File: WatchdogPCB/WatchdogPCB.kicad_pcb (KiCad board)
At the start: 2 copper layers, 5 parts, among them J1 Conn_01x05_Socket, J2 Conn_01x05_Pin, J3 Screw_Terminal_01x03, J4 Power

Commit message: Layout mostly done
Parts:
- added D1: 5.1V, Diode_THT:D_A-405_P10.16mm_Horizontal, F.Cu at (101.6, 94.0)
- added D2: 1N5404, Diode_THT:D_DO-201AD_P15.24mm_Horizontal, F.Cu at (127.0, 38.1)
- added F1: 3A, Fuse:Fuse_Blade_ATO_directSolder, F.Cu at (103.3, 38.1)
- added H1: MountingHole, MountingHole:MountingHole_3.2mm_M3_Pad, F.Cu at (147.3, 109.2)
- added H2: MountingHole, MountingHole:MountingHole_3.2mm_M3_Pad, F.Cu at (104.1, 106.7)
- added H3: MountingHole, MountingHole:MountingHole_3.2mm_M3_Pad, F.Cu at (144.8, 38.1)
- added H4: MountingHole, MountingHole:MountingHole_3.2mm_M3_Pad, F.Cu at (91.4, 55.9)
- added J5: Thermistor 1, TerminalBlock:TerminalBlock_bornier-2_P5.08mm, F.Cu at (83.8, 99.1)
- added J6: Thermistor 2, TerminalBlock:TerminalBlock_bornier-2_P5.08mm, F.Cu at (83.8, 109.2)
- added J7: Dashboard A, Connector_JST:JST_XH_B3B-XH-A_1x03_P2.50mm_Vertical, F.Cu at (147.3, 78.7)
- added J8: Dashboard B, Connector_JST:JST_XH_B5B-XH-A_1x05_P2.50mm_Vertical, F.Cu at (147.3, 96.4)
- added JP1: 5V jumper, Connector_PinSocket_2.54mm:PinSocket_1x02_P2.54mm_Vertical, F.Cu at (137.2, 63.5)
- added JP2: 12V jumper, Connector_PinSocket_2.54mm:PinSocket_1x02_P2.54mm_Vertical, F.Cu at (132.1, 40.6)
- added R1: 4.7k, Resistor_THT:R_Axial_DIN0207_L6.3mm_D2.5mm_P7.62mm_Horizontal, F.Cu at (101.6, 48.3)
- added R10: 470, Resistor_THT:R_Axial_DIN0207_L6.3mm_D2.5mm_P7.62mm_Horizontal, F.Cu at (134.6, 99.1)
- added R11: 4.7k, Resistor_THT:R_Axial_DIN0207_L6.3mm_D2.5mm_P7.62mm_Horizontal, F.Cu at (137.2, 99.1)
- added R12: 4.7k, Resistor_THT:R_Axial_DIN0207_L6.3mm_D2.5mm_P7.62mm_Horizontal, F.Cu at (142.2, 96.5)
- added R2: 1k, Resistor_THT:R_Axial_DIN0207_L6.3mm_D2.5mm_P7.62mm_Horizontal, F.Cu at (88.9, 94.0)
- added R3: 120k, Resistor_THT:R_Axial_DIN0207_L6.3mm_D2.5mm_P7.62mm_Horizontal, F.Cu at (106.7, 48.3)
- added R4: 4.7k, Resistor_THT:R_Axial_DIN0207_L6.3mm_D2.5mm_P7.62mm_Horizontal, F.Cu at (91.4, 94.0)
- added R5: 100k, Resistor_THT:R_Axial_DIN0207_L6.3mm_D2.5mm_P7.62mm_Horizontal, F.Cu at (121.9, 88.9)
- added R6: 39k, Resistor_THT:R_Axial_DIN0207_L6.3mm_D2.5mm_P7.62mm_Horizontal, F.Cu at (119.4, 96.5)
- added R7: 1k, Resistor_THT:R_Axial_DIN0207_L6.3mm_D2.5mm_P7.62mm_Horizontal, F.Cu at (124.5, 101.6)
- added R8: 1k, Resistor_THT:R_Axial_DIN0207_L6.3mm_D2.5mm_P7.62mm_Horizontal, F.Cu at (121.9, 99.1)
- added R9: 470, Resistor_THT:R_Axial_DIN0207_L6.3mm_D2.5mm_P7.62mm_Horizontal, F.Cu at (132.1, 104.1)
- added RV1: 10k, Potentiometer_THT:Potentiometer_Piher_PT-10-V10_Vertical_Hole, F.Cu at (144.8, 48.3)
- added U2: MCP602, Package_DIP:DIP-8_W7.62mm_Socket_LongPads, F.Cu at (116.8, 48.3)
- added U3: DS3695N, Package_DIP:DIP-8_W7.62mm_Socket_LongPads, F.Cu at (106.7, 66.0)
- J1: value Conn_01x05_Socket -> Roll hoop; footprint Connector_Molex:Molex_KK-254_AE-6410-05A_1x05_P2.54mm_Vertical -> TerminalBlock:TerminalBlock_bornier-4_P5.08mm
- J2: value Conn_01x05_Pin -> Speed & Oil; footprint Connector_PinHeader_2.54mm:PinHeader_1x05_P2.54mm_Vertical -> TerminalBlock:TerminalBlock_bornier-4_P5.08mm
- J3: value Screw_Terminal_01x03 -> H bridge driver control; footprint TerminalBlock:TerminalBlock_bornier-3_P5.08mm -> Connector_PinHeader_2.54mm:PinHeader_1x05_P2.54mm_Vertical
- moved J4 49.8 mm to (83.8, 38.1), turned to -90 degrees
- moved J1 48.9 mm to (83.8, 58.4), turned to -90 degrees
- moved J3 47.2 mm to (139.7, 63.5)
- moved A1 40.2 mm to (111.8, 73.7)
- moved J2 28.0 mm to (83.8, 78.7), turned to -90 degrees
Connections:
- A1 pad 1: unconnected-(A1-D1/TX-Pad1) -> Net-(A1-D1/TX)
- A1 pad 10: unconnected-(A1-D7-Pad10) -> Net-(A1-D7)
- A1 pad 11: unconnected-(A1-D8-Pad11) -> Net-(A1-D8)
- A1 pad 14: unconnected-(A1-D11-Pad14) -> Net-(A1-D11)
- A1 pad 19: unconnected-(A1-A0-Pad19) -> Net-(A1-A0)
- A1 pad 2: unconnected-(A1-D0/RX-Pad2) -> Net-(A1-D0/RX)
- A1 pad 20: unconnected-(A1-A1-Pad20) -> Net-(A1-A1)
- A1 pad 21: unconnected-(A1-A2-Pad21) -> Net-(A1-A2)
- A1 pad 22: unconnected-(A1-A3-Pad22) -> /Button
- A1 pad 23: unconnected-(A1-A4-Pad23) -> /SDA
- A1 pad 24: unconnected-(A1-A5-Pad24) -> /SCL
- A1 pad 27: unconnected-(A1-+5V-Pad27) -> +5V
- A1 pad 29: unconnected-(A1-GND-Pad29) -> GND
- A1 pad 30: unconnected-(A1-VIN-Pad30) -> Net-(A1-VIN)
- A1 pad 4: unconnected-(A1-GND-Pad4) -> GND
- A1 pad 5: unconnected-(A1-D2-Pad5) -> Net-(A1-D2)
- A1 pad 6: unconnected-(A1-D3-Pad6) -> Net-(A1-D3)
- A1 pad 7: unconnected-(A1-D4-Pad7) -> Net-(A1-D4)
- A1 pad 8: unconnected-(A1-D5-Pad8) -> Net-(A1-D5)
- A1 pad 9: unconnected-(A1-D6-Pad9) -> Net-(A1-D6)
- J1 pad 1: unconnected-(J1-Pin_1-Pad1) -> Net-(J1-Pin_1)
- J1 pad 2: unconnected-(J1-Pin_2-Pad2) -> Net-(J1-Pin_2)
- J1 pad 3: unconnected-(J1-Pin_3-Pad3) -> +12V
- J1 pad 4: unconnected-(J1-Pin_4-Pad4) -> GND
- J2 pad 1: unconnected-(J2-Pin_1-Pad1) -> +5V
- J2 pad 2: unconnected-(J2-Pin_2-Pad2) -> /Hall effect
- J2 pad 3: unconnected-(J2-Pin_3-Pad3) -> GND
- J2 pad 4: unconnected-(J2-Pin_4-Pad4) -> /Oil
- J3 pad 1: unconnected-(J3-Pin_1-Pad1) -> Net-(J3-Pin_1)
- J3 pad 2: unconnected-(J3-Pin_2-Pad2) -> Net-(A1-D3)
- J3 pad 3: unconnected-(J3-Pin_3-Pad3) -> Net-(A1-D5)
- J4 pad 1: Net-(J4-Pin_1) -> /Power in
- J4 pad 2: Net-(J4-Pin_2) -> +12V
- J4 pad 3: Net-(J4-Pin_1) -> GND
- J4 pad 4: Net-(J4-Pin_2) -> GND
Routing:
- net GND: track 0.00 -> 303.2 mm, vias 0 -> 28
- net +5V: track 0.00 -> 209.4 mm, vias 0 -> 14
- net +12V: track 0.00 -> 86.5 mm, vias 0 -> 4
- net Net-(A1-D11): track 0.00 -> 79.8 mm, vias 0 -> 4
- net Net-(J6-Pin_1): track 0.00 -> 76.2 mm, vias 0 -> 5
- net +BATT: track 0.00 -> 67.9 mm
- net Net-(J5-Pin_1): track 0.00 -> 63.5 mm, vias 0 -> 3
- net Net-(A1-D5): track 0.00 -> 61.0 mm, vias 0 -> 2
- net /Hall effect: track 0.00 -> 59.6 mm, vias 0 -> 2
- net Net-(A1-VIN): track 0.00 -> 50.7 mm, vias 0 -> 3
- net Net-(A1-D6): track 0.00 -> 49.3 mm, vias 0 -> 2
- net Net-(A1-D3): track 0.00 -> 48.3 mm, vias 0 -> 2
- net Net-(A1-D2): track 0.00 -> 46.3 mm
- net Net-(A1-D7): track 0.00 -> 45.7 mm, vias 0 -> 2
- net Net-(A1-D4): track 0.00 -> 40.6 mm, vias 0 -> 2
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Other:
- board outline added: 78.7 x 88.9 mm
- copper layers 2 -> 4

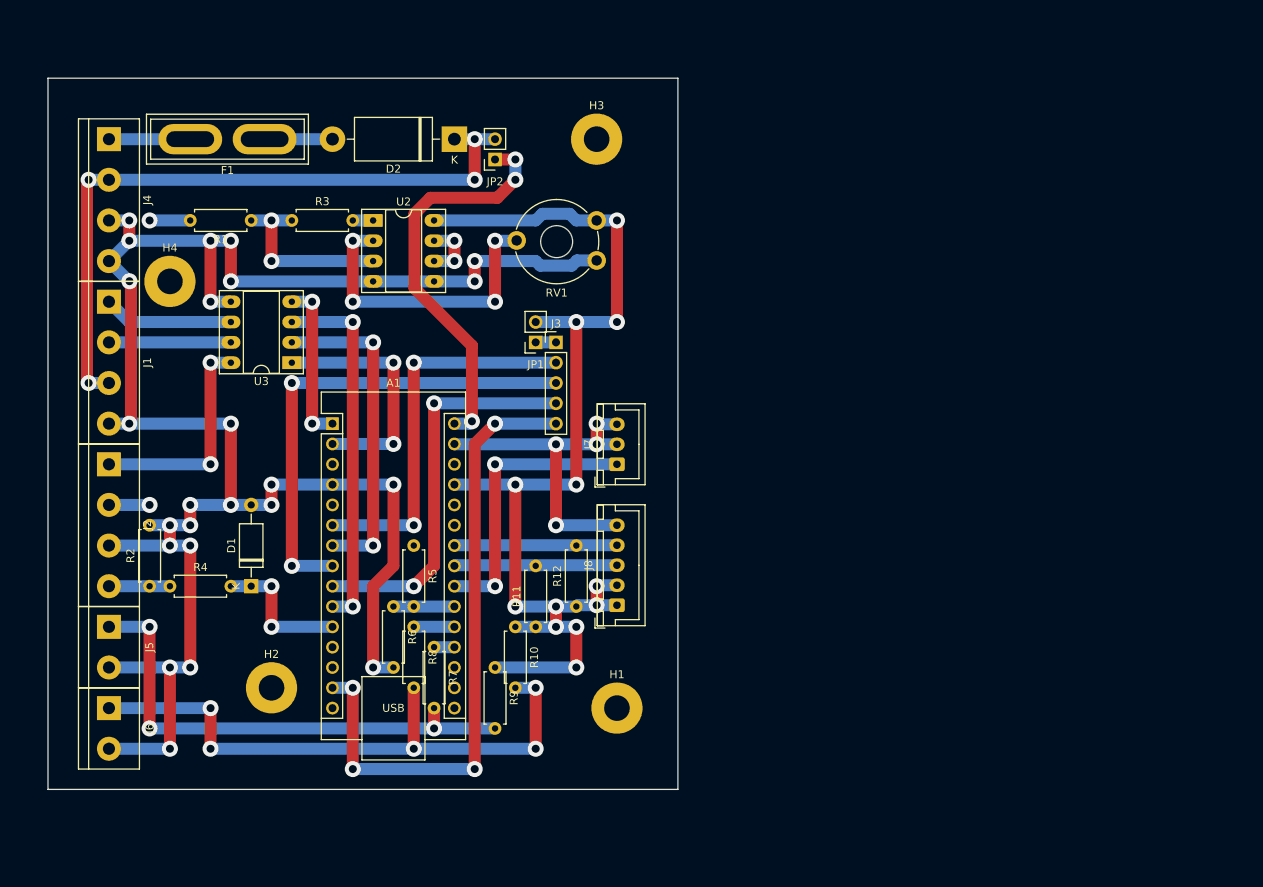
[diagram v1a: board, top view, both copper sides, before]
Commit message: Made fold go in two parts
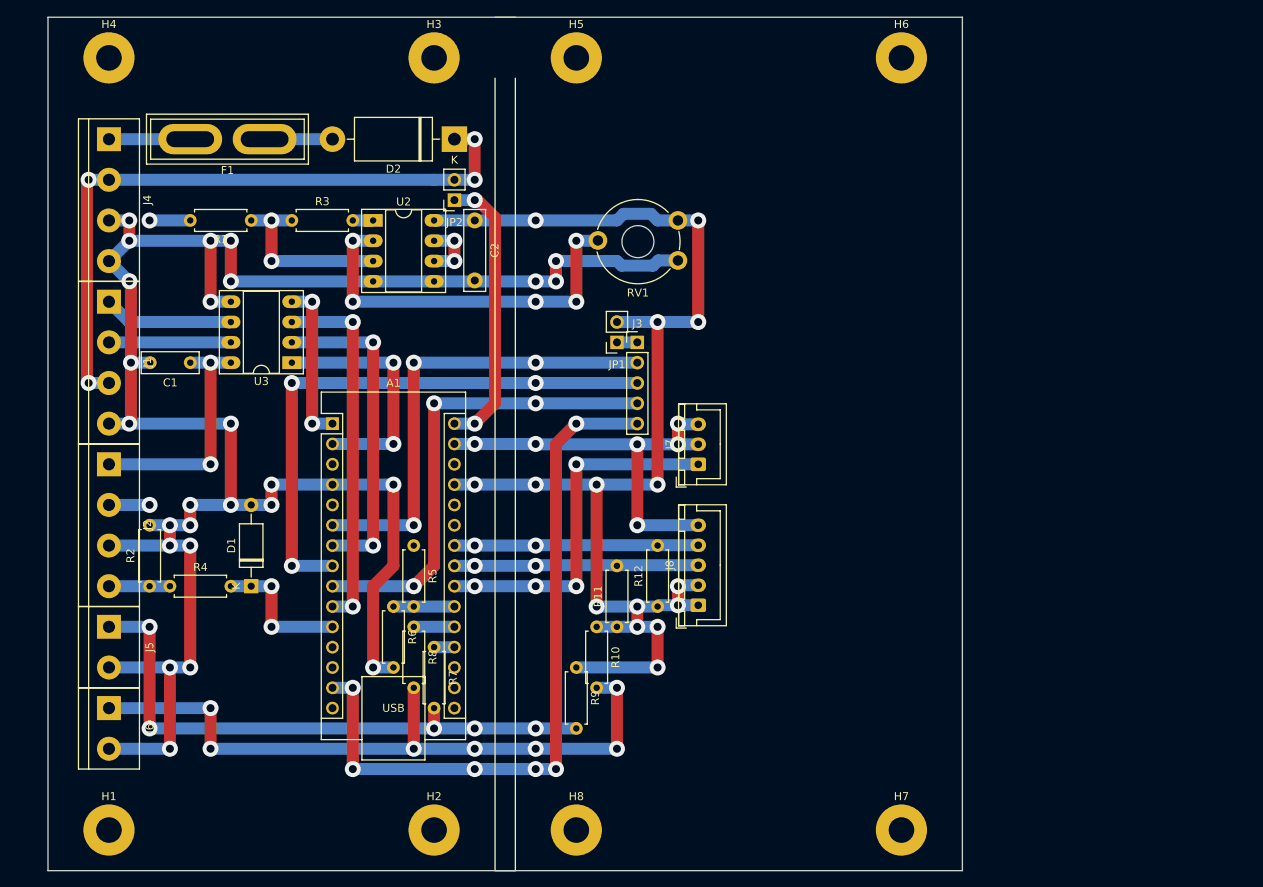
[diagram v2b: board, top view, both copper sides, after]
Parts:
- added C1: 10n, Capacitor_THT:C_Rect_L7.0mm_W2.5mm_P5.00mm, F.Cu at (94.0, 66.0)
- added C2: 10n, Capacitor_THT:C_Rect_L10.0mm_W2.5mm_P7.50mm_MKS4, F.Cu at (129.5, 48.3)
- added H5: MountingHole, MountingHole:MountingHole_3.2mm_M3_Pad, F.Cu at (142.2, 27.9)
- added H6: MountingHole, MountingHole:MountingHole_3.2mm_M3_Pad, F.Cu at (182.9, 27.9)
- added H7: MountingHole, MountingHole:MountingHole_3.2mm_M3_Pad, F.Cu at (182.9, 124.5)
- added H8: MountingHole, MountingHole:MountingHole_3.2mm_M3_Pad, F.Cu at (142.2, 124.5)
- moved H1 65.3 mm to (83.8, 124.5)
- moved H4 29.0 mm to (83.8, 27.9)
- moved H2 27.0 mm to (124.5, 124.5)
- moved H3 22.7 mm to (124.5, 27.9)
- moved J3 10.2 mm to (149.9, 63.5)
- moved J7 10.2 mm to (157.5, 78.7)
- moved J8 10.2 mm to (157.5, 96.4)
- moved JP1 10.2 mm to (147.3, 63.5)
- moved R10 10.2 mm to (144.8, 99.1)
- moved R11 10.2 mm to (147.3, 99.1)
- moved R12 10.2 mm to (152.4, 96.5)
- moved R9 10.2 mm to (142.2, 104.1)
- moved RV1 10.2 mm to (154.9, 48.3)
- moved JP2 7.18 mm to (127.0, 45.7)
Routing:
- net +5V: track 209.4 -> 232.2 mm, vias 14 -> 17
- net GND: track 303.2 -> 326.0 mm, vias 28 -> 32
- net Net-(A1-VIN): track 50.7 -> 35.3 mm, vias 3 -> 2
- net Net-(A1-D11): track 79.8 -> 90.5 mm, vias 4 -> 6
- net /SDA: track 20.4 -> 30.6 mm, vias 0 -> 2
- net /SCL: track 20.3 -> 30.6 mm, vias 0 -> 2
- net Net-(A1-D6): track 49.3 -> 59.5 mm, vias 2 -> 3
- net Net-(A1-D5): track 61.0 -> 71.1 mm, vias 2 -> 3
- net Net-(A1-D3): track 48.3 -> 58.4 mm, vias 2 -> 3
- net Net-(J6-Pin_1): track 76.2 -> 86.4 mm, vias 5 -> 7
- net Net-(J5-Pin_1): track 63.5 -> 73.7 mm, vias 3 -> 5
- net /Threshold adjust: track 38.3 -> 48.4 mm, vias 4 -> 5
- net /Button: track 35.6 -> 45.7 mm, vias 2 -> 4
- net +12V: track 86.5 -> 84.0 mm
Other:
- board size 78.7 x 88.9 mm -> 114.3 x 106.7 mm

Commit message: Board layout as contructed
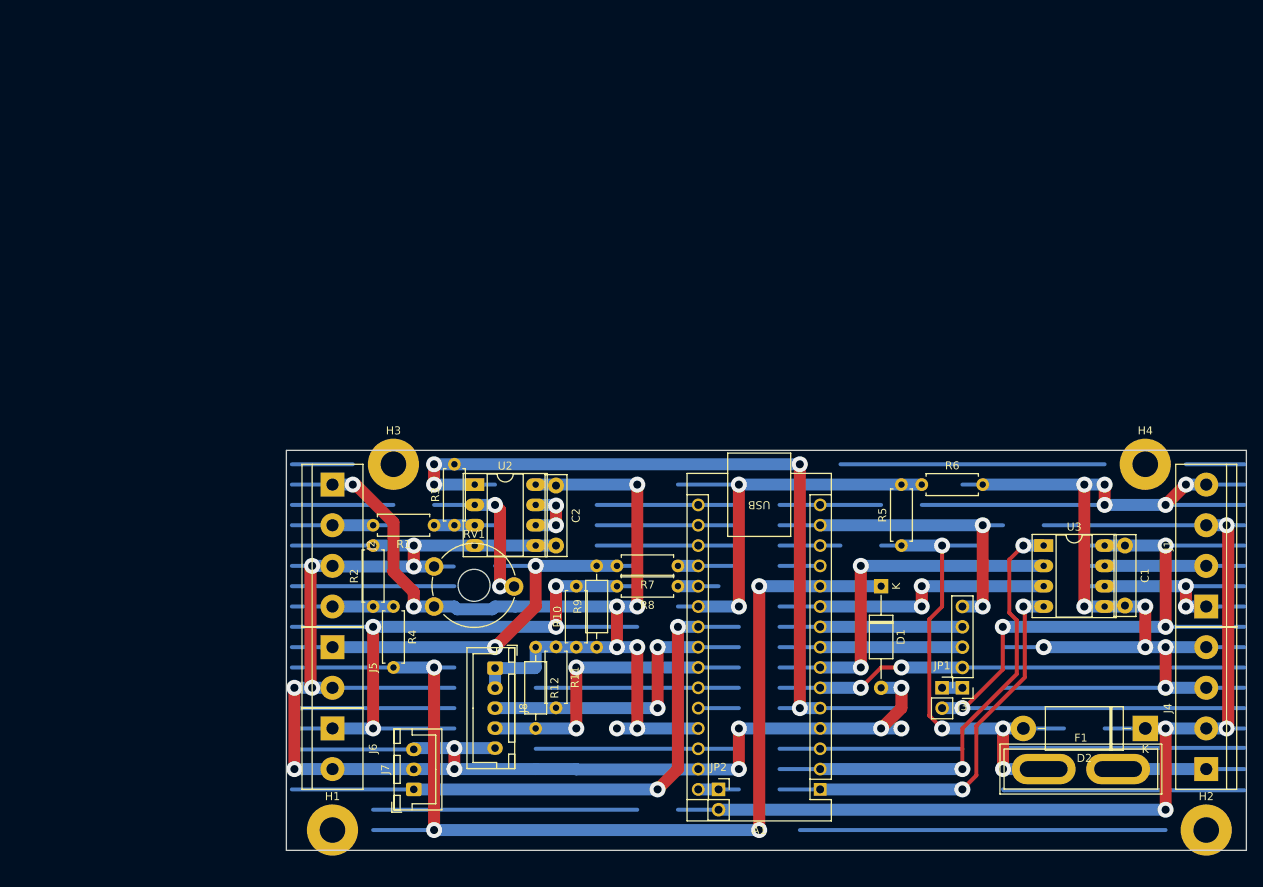
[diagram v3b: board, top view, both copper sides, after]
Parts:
- removed H5, H6, H7, H8: MountingHole, MountingHole:MountingHole_3.2mm_M3_Pad
- C1: footprint Capacitor_THT:C_Rect_L7.0mm_W2.5mm_P5.00mm -> Capacitor_THT:C_Rect_L10.0mm_W2.5mm_P7.50mm_MKS4
- D1: footprint Diode_THT:D_A-405_P10.16mm_Horizontal -> Diode_THT:D_A-405_P12.70mm_Horizontal
- R12, R9: footprint Resistor_THT:R_Axial_DIN0207_L6.3mm_D2.5mm_P7.62mm_Horizontal -> Resistor_THT:R_Axial_DIN0207_L6.3mm_D2.5mm_P10.16mm_Horizontal
- moved J4 158.2 mm to (221.0, 116.8), turned to 90 degrees
- moved J1 142.4 mm to (221.0, 96.5), turned to 90 degrees
- moved H4 139.1 mm to (213.4, 78.7)
- moved F1 125.2 mm to (200.7, 116.8), turned to 0 degrees
- moved C1 119.1 mm to (210.8, 88.9), turned to -90 degrees
- moved D2 113.5 mm to (213.4, 111.8)
- moved U3 96.7 mm to (200.7, 88.9), turned to 0 degrees
- moved H2 96.5 mm to (221.0, 124.5)
- moved JP2 80.7 mm to (160.0, 119.4), turned to 0 degrees
- moved D1 78.7 mm to (180.3, 94.0), turned to -90 degrees
- moved A1 76.2 mm to (172.7, 119.4), turned to 180 degrees
- moved R6 67.8 mm to (185.4, 81.3), turned to 0 degrees
- moved R5 61.0 mm to (182.9, 88.9), turned to 90 degrees
- moved JP1 59.3 mm to (188.0, 106.7), turned to 0 degrees
- moved J3 59.3 mm to (190.5, 106.7), turned to 180 degrees
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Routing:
- net (no net): track 0.00 -> 240.5 mm
- net Net-(A1-D8): track 17.8 -> 134.6 mm, vias 2 -> 4
- net GND: track 326.0 -> 407.5 mm, vias 32 -> 24
- net +5V: track 232.2 -> 304.2 mm, vias 17 -> 13
- net Net-(A1-D2): track 46.3 -> 101.6 mm, vias 0 -> 4
- net +12V: track 84.0 -> 139.3 mm
- net Net-(A1-D11): track 90.5 -> 40.6 mm, vias 6 -> 2
- net Net-(A1-D5): track 71.1 -> 22.9 mm, vias 3 -> 0
- net /Hall effect: track 59.6 -> 12.7 mm, vias 2 -> 0
- net Net-(A1-A2): track 7.62 -> 53.3 mm, vias 0 -> 2
- net Net-(A1-D6): track 59.5 -> 22.9 mm, vias 3 -> 0
- net Net-(A1-D1/TX): track 20.3 -> 51.6 mm
- net Net-(A1-VIN): track 35.3 -> 5.08 mm, vias 2 -> 0
- net /Button: track 45.7 -> 74.7 mm, vias 4 -> 2
- net /Threshold adjust: track 48.4 -> 19.8 mm, vias 5 -> 2
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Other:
- board size 114.3 x 106.7 mm -> 120 x 50 mm

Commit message: Added button to UI
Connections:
- net Net-(A1-D11) renamed /Aux
- net Net-(A1-D3) renamed /Motor A
- net Net-(A1-D5) renamed /Motor B
- net Net-(A1-D6) renamed /Horn
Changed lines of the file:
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@@
     (aux_axis_origin 111.76 81.28)
     (pcbplotparams
-      (layerselection 0x00010fc_ffffffff)
-      (plot_on_all_layers_selection 0x0000000_00000000)
+      (layerselection 0x0001000_7ffffff8)
+      (plot_on_all_layers_selection 0x0001800_00000007)
       (disableapertmacros false)
       (usegerberextensions false)
@@
       (sketchpadsonfab false)
       (subtractmaskfromsilk false)
-      (outputformat 1)
-      (mirror false)
-      (drillshape 1)
+      (outputformat 5)
+      (mirror true)
+      (drillshape 2)
       (scaleselection 1)
-      (outputdirectory "")
+      (outputdirectory "output/output2/")
     )
   )
@@
   (net 4 "GND")
   (net 5 "Net-(A1-D2)")
-  (net 6 "Net-(A1-D3)")
+  (net 6 "/Motor A")
   (net 7 "unconnected-(A1-D9-Pad12)")
   (net 8 "unconnected-(A1-D10-Pad13)")
@@
   (net 11 "unconnected-(A1-D13-Pad16)")
   (net 12 "unconnected-(A1-3V3-Pad17)")
-  (net 13 "Net-(A1-D5)")
-  (net 14 "Net-(A1-D6)")
+  (net 13 "/Motor B")
+  (net 14 "/Horn")
   (net 15 "Net-(A1-D7)")
   (net 16 "unconnected-(A1-A6-Pad25)")
   (net 17 "unconnected-(A1-~{RESET}-Pad28)")
   (net 18 "Net-(A1-D8)")
-  (net 19 "Net-(A1-D11)")
+  (net 19 "/Aux")
   (net 20 "Net-(A1-A0)")
   (net 21 "Net-(A1-A1)")
@@
       (net 5 "Net-(A1-D2)") (pinfunction "D2") (pintype "bidirectional"))
     (pad "6" thru_hole oval (at 0 12.7 180) (size 1.6 1.6) (drill 1) (layers "*.Cu" "*.Mask")
-      (net 6 "Net-(A1-D3)") (pinfunction "D3") (pintype "bidirectional"))
+      (net 6 "/Motor A") (pinfunction "D3") (pintype "bidirectional"))
     (pad "7" thru_hole oval (at 0 15.24 180) (size 1.6 1.6) (drill 1) (layers "*.Cu" "*.Mask")
       (net 9 "Net-(A1-D4)") (pinfunction "D4") (pintype "bidirectional"))
     (pad "8" thru_hole oval (at 0 17.78 180) (size 1.6 1.6) (drill 1) (layers "*.Cu" "*.Mask")
-      (net 13 "Net-(A1-D5)") (pinfunction "D5") (pintype "bidirectional"))
+      (net 13 "/Motor B") (pinfunction "D5") (pintype "bidirectional"))
     (pad "9" thru_hole oval (at 0 20.32 180) (size 1.6 1.6) (drill 1) (layers "*.Cu" "*.Mask")
-      (net 14 "Net-(A1-D6)") (pinfunction "D6") (pintype "bidirectional"))
+      (net 14 "/Horn") (pinfunction "D6") (pintype "bidirectional"))
     (pad "10" thru_hole oval (at 0 22.86 180) (size 1.6 1.6) (drill 1) (layers "*.Cu" "*.Mask")
       (net 15 "Net-(A1-D7)") (pinfunction "D7") (pintype "bidirectional"))
@@
       (net 8 "unconnected-(A1-D10-Pad13)") (pinfunction "D10") (pintype "bidirectional+no_connect"))
     (pad "14" thru_hole oval (at 0 33.02 180) (size 1.6 1.6) (drill 1) (layers "*.Cu" "*.Mask")
-      (net 19 "Net-(A1-D11)") (pinfunction "D11") (pintype "bidirectional"))
+      (net 19 "/Aux") (pinfunction "D11") (pintype "bidirectional"))
     (pad "15" thru_hole oval (at 0 35.56 180) (size 1.6 1.6) (drill 1) (layers "*.Cu" "*.Mask")
       (net 10 "unconnected-(A1-D12-Pad15)") (pinfunction "D12") (pintype "bidirectional+no_connect"))
@@
       (net 37 "Net-(J3-Pin_1)") (pinfunction "Pin_1") (pintype "passive"))
     (pad "2" thru_hole oval (at 0 2.54 180) (size 1.7 1.7) (drill 1) (layers "*.Cu" "*.Mask")
-      (net 6 "Net-(A1-D3)") (pinfunction "Pin_2") (pintype "passive"))
+      (net 6 "/Motor A") (pinfunction "Pin_2") (pintype "passive"))
     (pad "3" thru_hole oval (at 0 5.08 180) (size 1.7 1.7) (drill 1) (layers "*.Cu" "*.Mask")
-      (net 13 "Net-(A1-D5)") (pinfunction "Pin_3") (pintype "passive"))
+      (net 13 "/Motor B") (pinfunction "Pin_3") (pintype "passive"))
     (pad "4" thru_hole oval (at 0 7.62 180) (size 1.7 1.7) (drill 1) (layers "*.Cu" "*.Mask")
-      (net 14 "Net-(A1-D6)") (pinfunction "Pin_4") (pintype "passive"))
+      (net 14 "/Horn") (pinfunction "Pin_4") (pintype "passive"))
     (pad "5" thru_hole oval (at 0 10.16 180) (size 1.7 1.7) (drill 1) (layers "*.Cu" "*.Mask")
-      (net 19 "Net-(A1-D11)") (pinfunction "Pin_5") (pintype "passive"))
+      (net 19 "/Aux") (pinfunction "Pin_5") (pintype "passive"))
     (model "${KICAD6_3DMODEL_DIR}/Connector_PinHeader_2.54mm.3dshapes/PinHeader_1x05_P2.54mm_Vertical.wrl"
       (offset (xyz 0 0 0))
